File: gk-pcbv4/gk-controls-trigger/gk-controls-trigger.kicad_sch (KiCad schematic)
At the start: 7 parts, among them J1 Conn_01x03, J2 Conn_01x01, J3 Conn_01x01, J4 Conn_01x01, J5 Conn_01x01

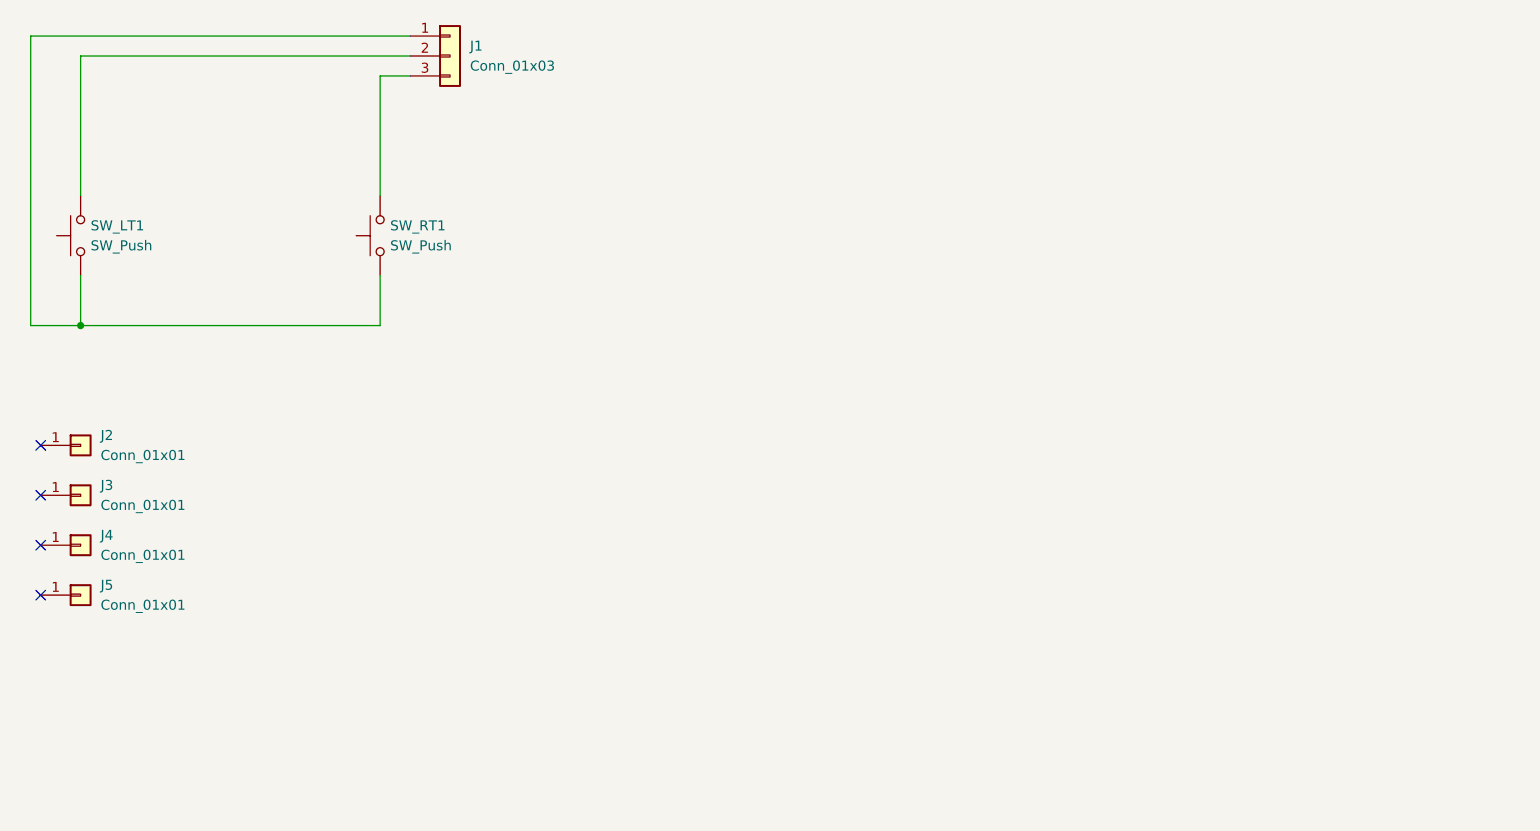
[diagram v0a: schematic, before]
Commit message: update controls layout triggers now are analog new ADC on control board Move bumper buttons to trigger daughterboard and put in more ergonomical position
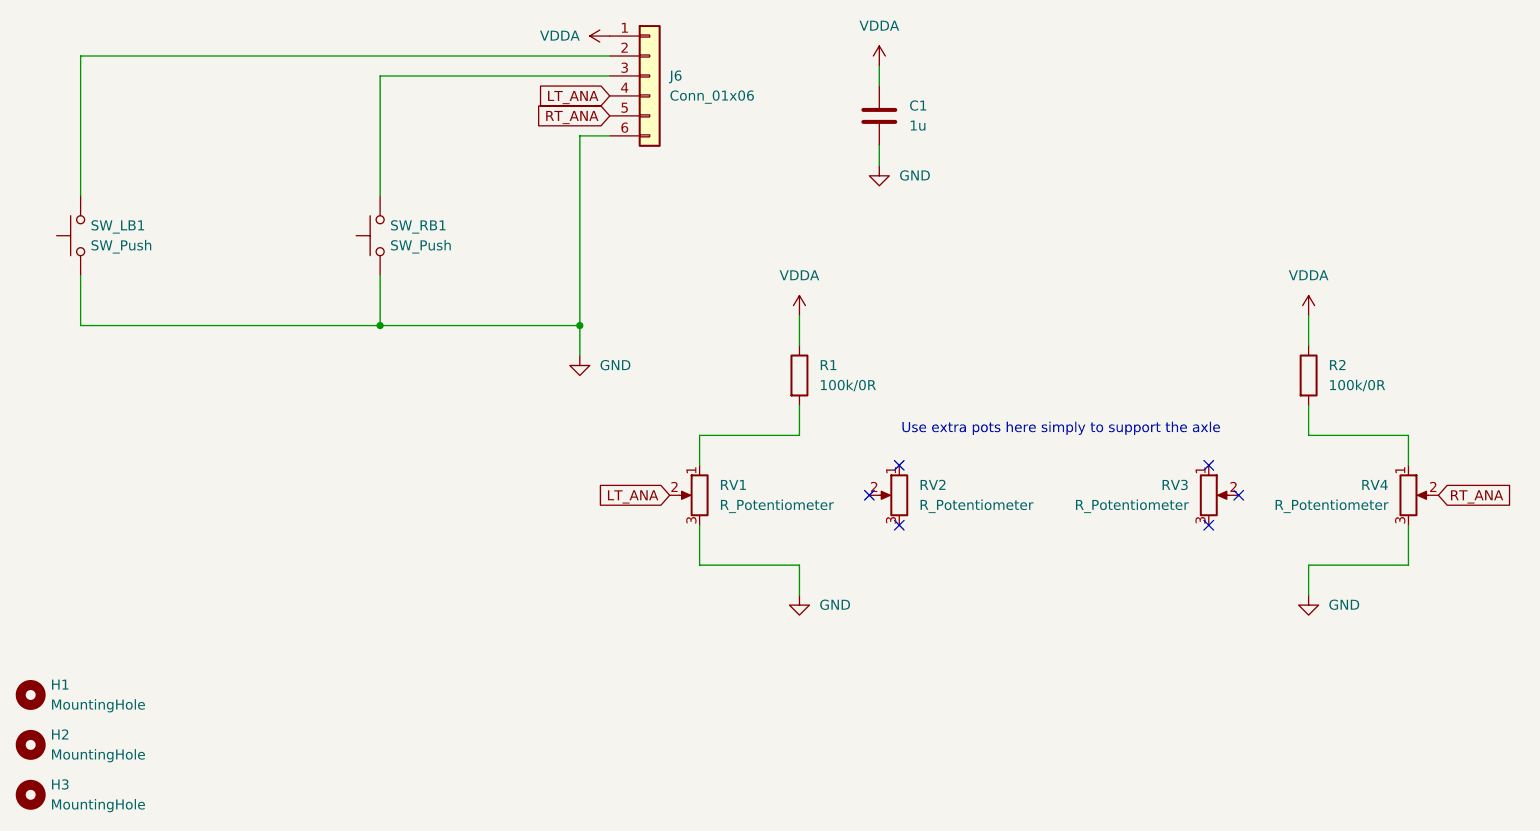
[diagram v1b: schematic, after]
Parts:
- removed J1: Conn_01x03, Connector_PinHeader_2.54mm:PinHeader_1x03_P2.54mm_Vertical, symbol Connector_Generic:Conn_01x03
- removed J2, J3, J4, J5: Conn_01x01, Connector_PinHeader_2.54mm:PinHeader_1x01_P2.54mm_Vertical, symbol Connector_Generic:Conn_01x01
- added C1: 1u, Capacitor_SMD:C_0603_1608Metric, symbol Device:C
- added H1, H2, H3: MountingHole, MountingHole:MountingHole_2.7mm_M2.5, symbol Mechanical:MountingHole
- added J6: Conn_01x06, Connector_FFC-FPC:TE_0-1734839-6_1x06-1MP_P0.5mm_Horizontal, symbol Connector_Generic:Conn_01x06
- added R1, R2: 100k/0R, Resistor_SMD:R_0603_1608Metric, symbol Device:R
- added RV1, RV2, RV3, RV4: R_Potentiometer, Potentiometer_THT:Potentiometer_Bourns_3266W_Vertical, symbol Device:R_Potentiometer
- renumbered SW_LT1 to SW_LB1, SW_RT1 to SW_RB1
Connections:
- net GND: now reaches SW_LB1.1, SW_RB1.1
- net GND: now also C1.2, J6.6 (Pin_6), RV1.3, RV4.3
- net at SW_LB1.2: now also J6.2 (Pin_2)
- net at SW_RB1.2: now also J6.3 (Pin_3)
- new net: R1.2, RV1.1
- new net: R2.2, RV4.1
- new net LT_ANA: J6.4 (Pin_4), RV1.2
- new net RT_ANA: J6.5 (Pin_5), RV4.2
- new net VDDA: C1.1, J6.1 (Pin_1), R1.1, R2.1
- no-connect marks 4 -> 6
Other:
- note added: "Use extra pots here simply to support the axle"
